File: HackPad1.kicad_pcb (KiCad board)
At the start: 2 copper layers, 3.3 x 3.6 mm, 25 parts, among them J1 Conn_01x04_Pin, SW1 SW_Push, SW10 RotaryEncoder, SW2 SW_Push, SW3 SW_Push, SW4 SW_Push, SW5 SW_Push, SW6 SW_Push, SW7 SW_Push, SW8 SW_Push, SW9 SW_Push, U1 MOUDLE-SEEEDUINO-XIAO

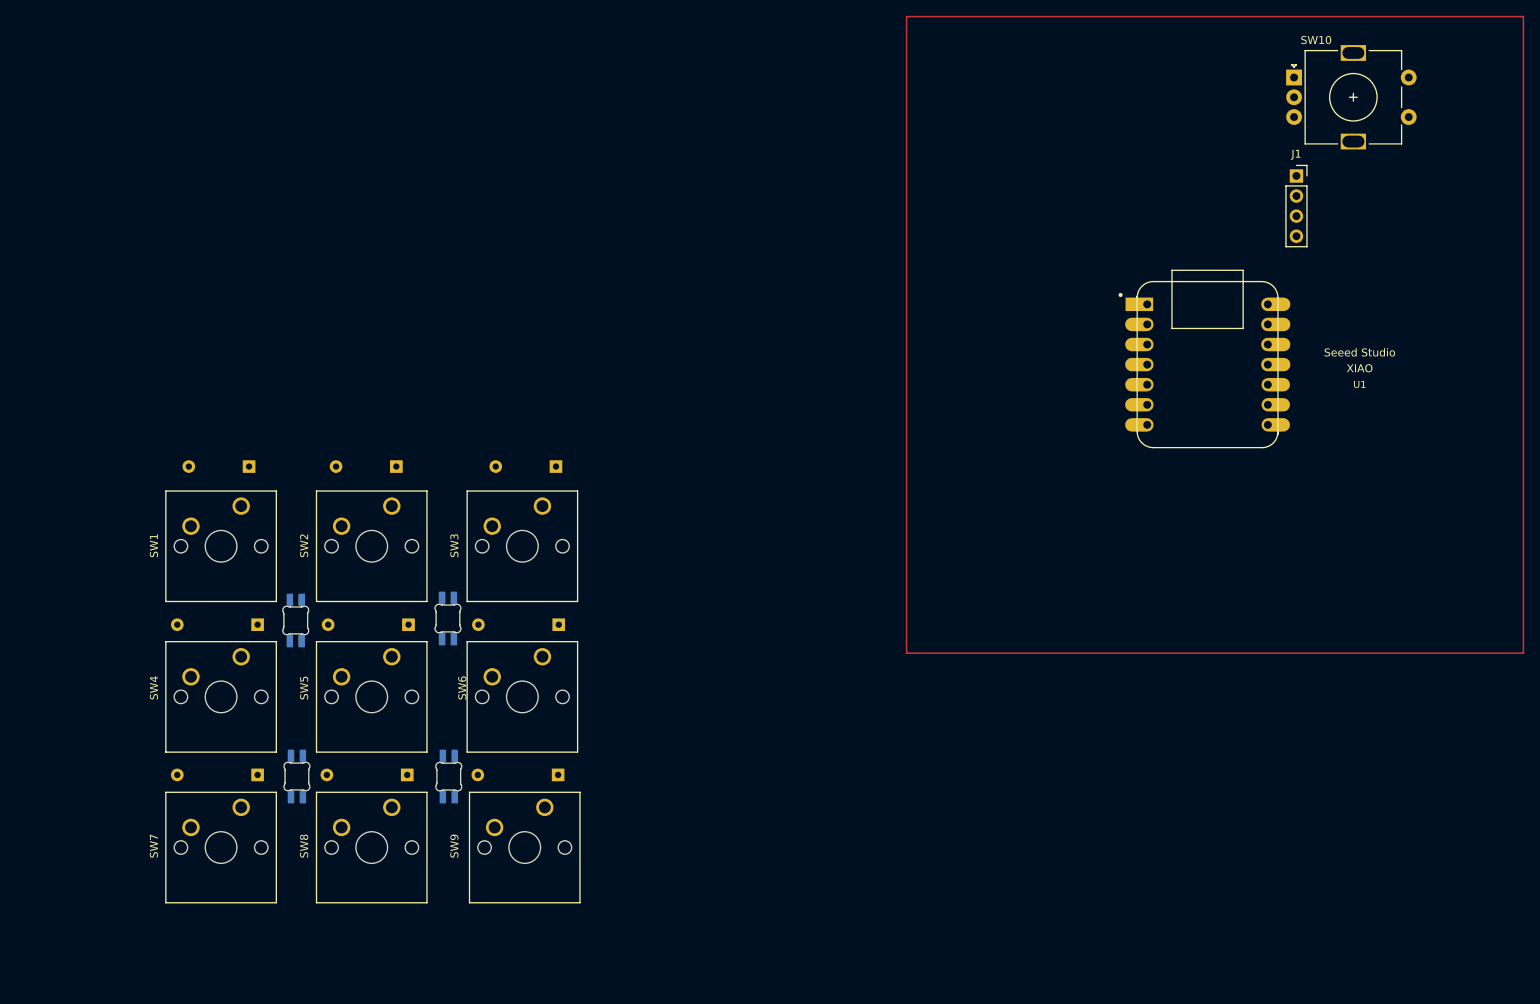
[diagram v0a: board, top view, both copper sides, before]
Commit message: added complete pcb layout need to start routing
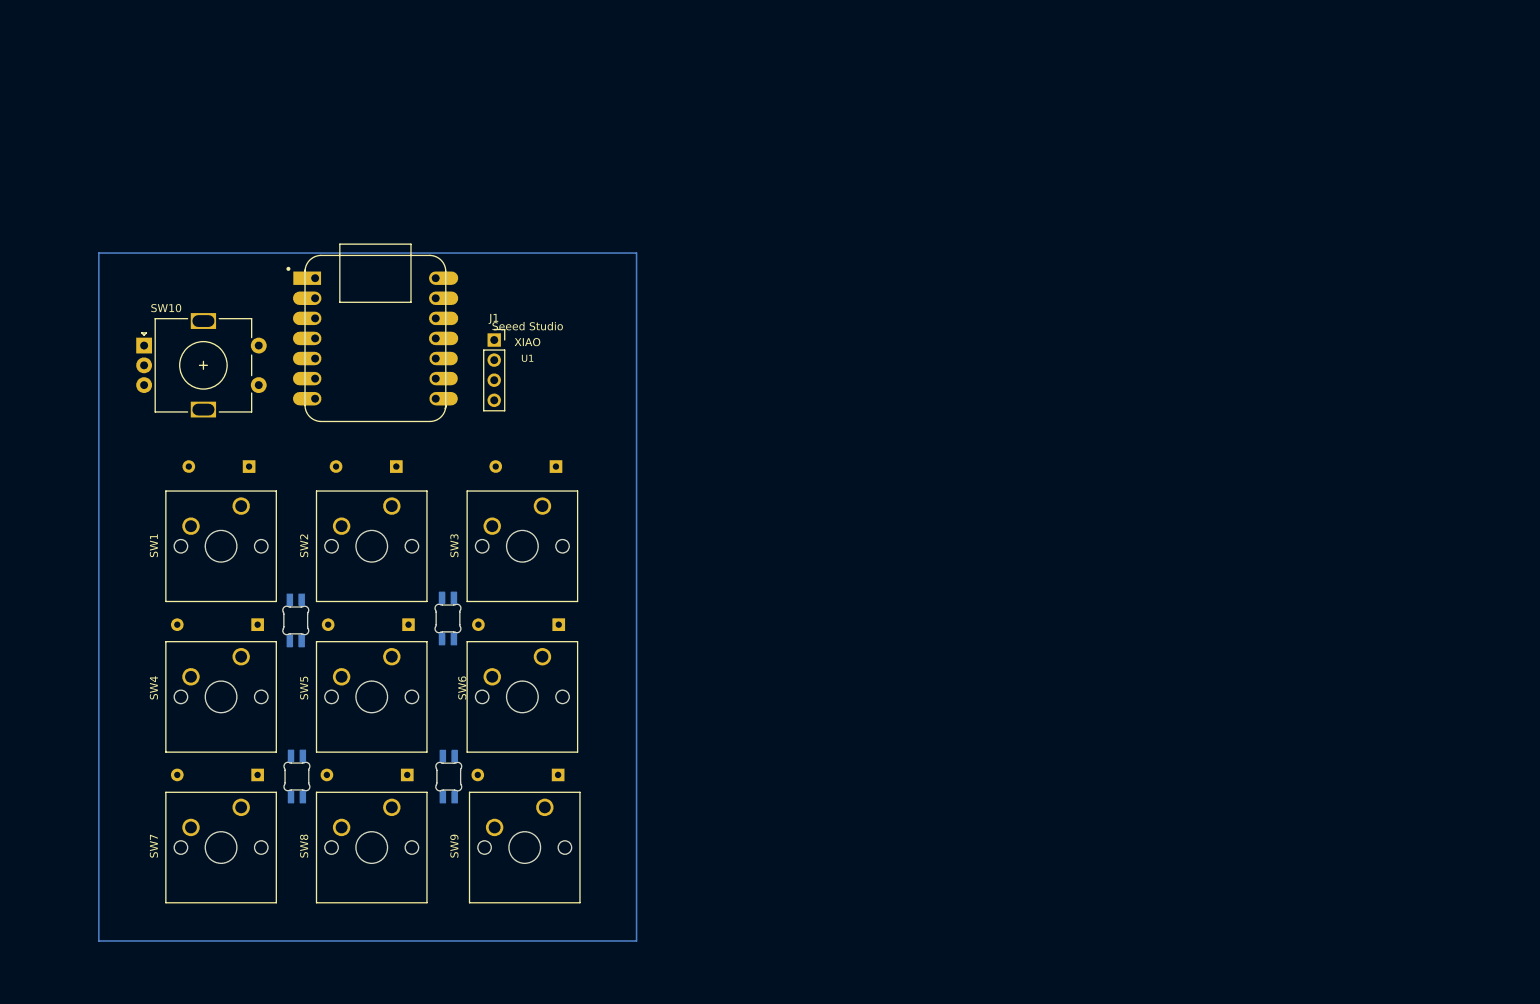
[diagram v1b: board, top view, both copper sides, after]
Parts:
- moved SW10 149.3 mm to (87.7, 79.7)
- moved U1 105.3 mm to (117.0, 78.8)
- moved J1 103.6 mm to (132.0, 79.0)
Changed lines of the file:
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@@
 	(footprint "Rotary_Encoder:RotaryEncoder_Alps_EC11E-Switch_Vertical_H20mm"
 		(layer "F.Cu")
-		(at 233.15 45.8)
+		(at 87.725 79.7)
 		(descr "Alps rotary encoder, EC12E... with switch, vertical shaft, http://www.alps.com/prod/info/E/HTML/Encoder/Incremental/EC11/EC11E15204A3.html")
 		(tags "rotary encoder")
@@
 	(footprint "Connector_PinSocket_2.54mm:PinSocket_1x04_P2.54mm_Vertical"
 		(layer "F.Cu")
-		(at 233.45 58.25)
+		(at 132 79)
 		(descr "Through hole straight socket strip, 1x04, 2.54mm pitch, single row (from Kicad 4.0.7), script generated")
 		(tags "Through hole socket strip THT 1x04 2.54mm single row")
@@
 	(footprint "footprints:XIAO-Generic-Hybrid-14P-2.54-21X17.8MM"
 		(layer "F.Cu")
-		(at 222.209 82.107531)
+		(at 116.975 78.8)
 		(property "Reference" "U1"
 			(at 19.25 2.54 0)
@@
 	)
 	(gr_rect
-		(start 184.15 38.1)
-		(end 262.15 118.6)
+		(start 82 68)
+		(end 150 155)
 		(locked yes)
 		(stroke
@@
 		)
 		(fill none)
-		(layer "F.Cu")
-		(net 23)
+		(layer "B.Cu")
 	)
 )

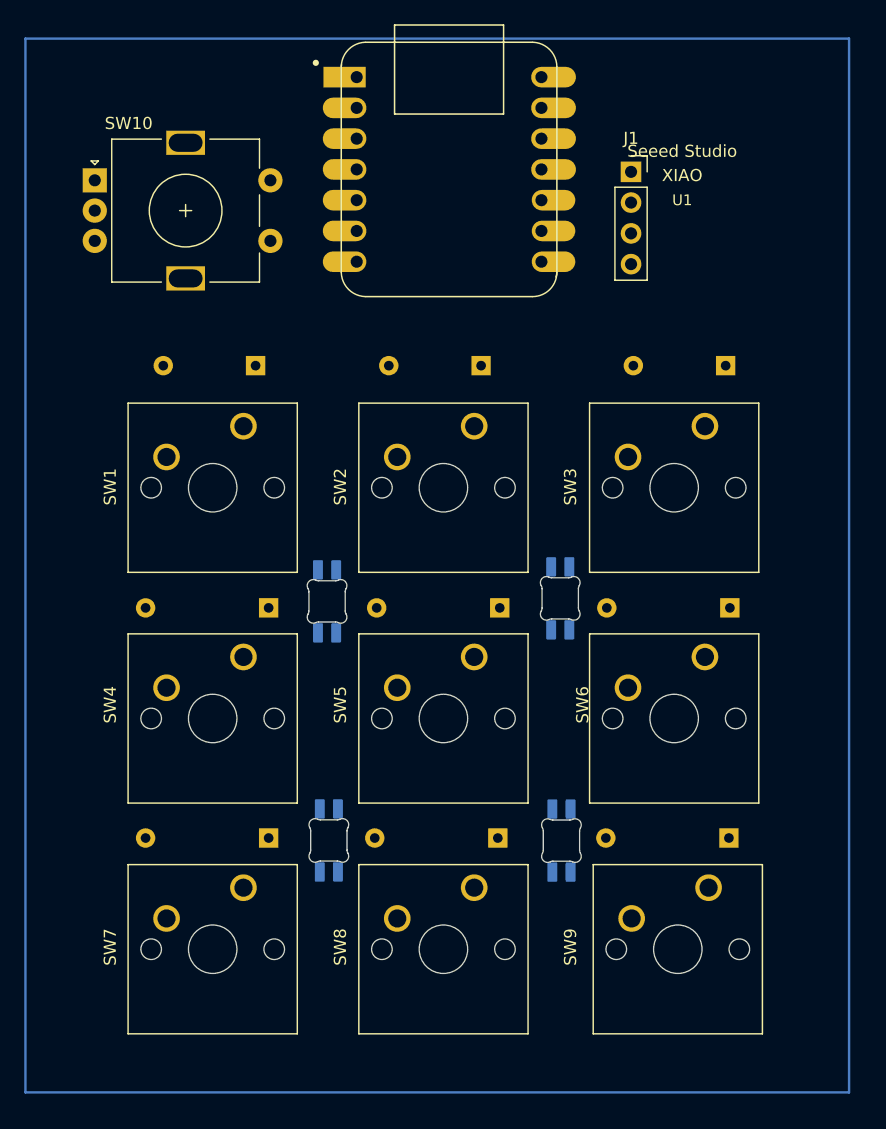
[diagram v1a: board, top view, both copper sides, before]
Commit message: added pcb edge cut
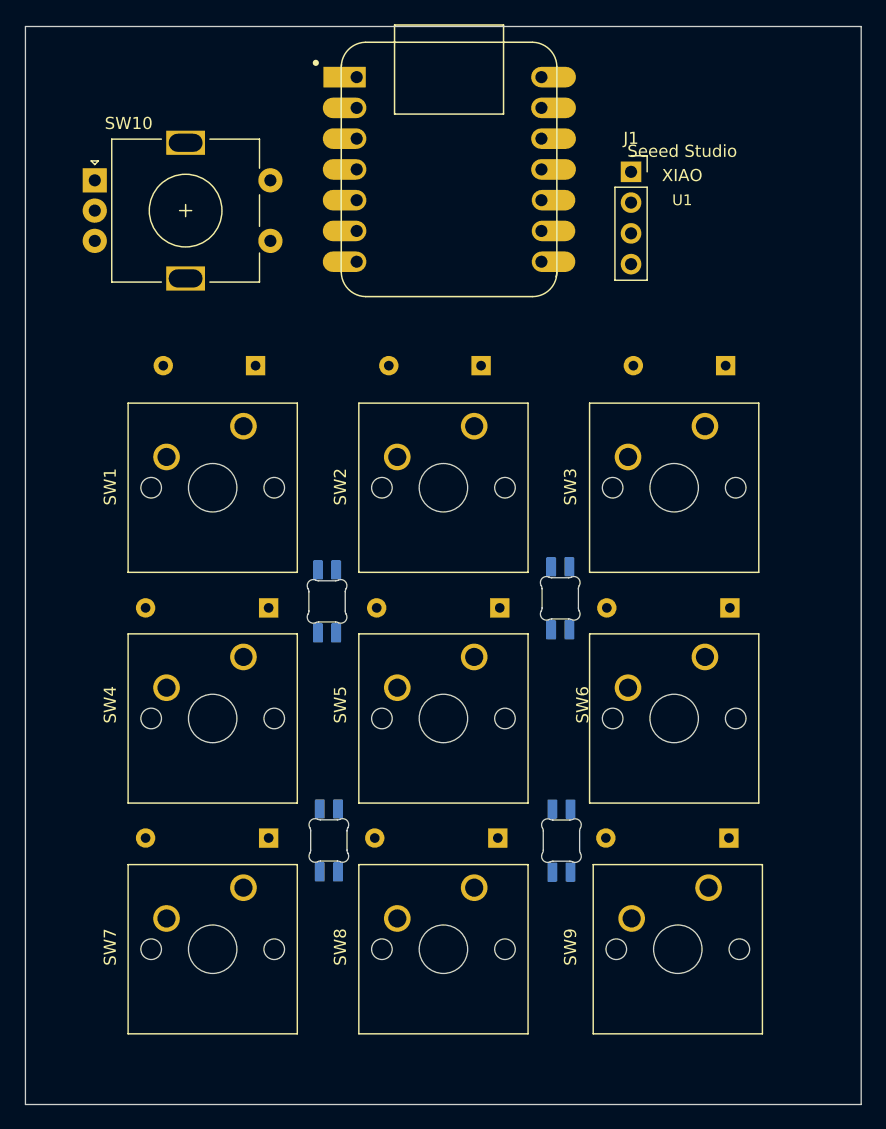
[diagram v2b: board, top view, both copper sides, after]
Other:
- board size 3.3 x 3.6 mm -> 69 x 89 mm
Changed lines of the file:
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@@
 	)
 	(gr_rect
-		(start 82 68)
-		(end 150 155)
-		(locked yes)
+		(start 82 67)
+		(end 151 156)
 		(stroke
-			(width 0.2)
+			(width 0.05)
 			(type default)
 		)
 		(fill none)
-		(layer "B.Cu")
+		(layer "Edge.Cuts")
 	)
 )

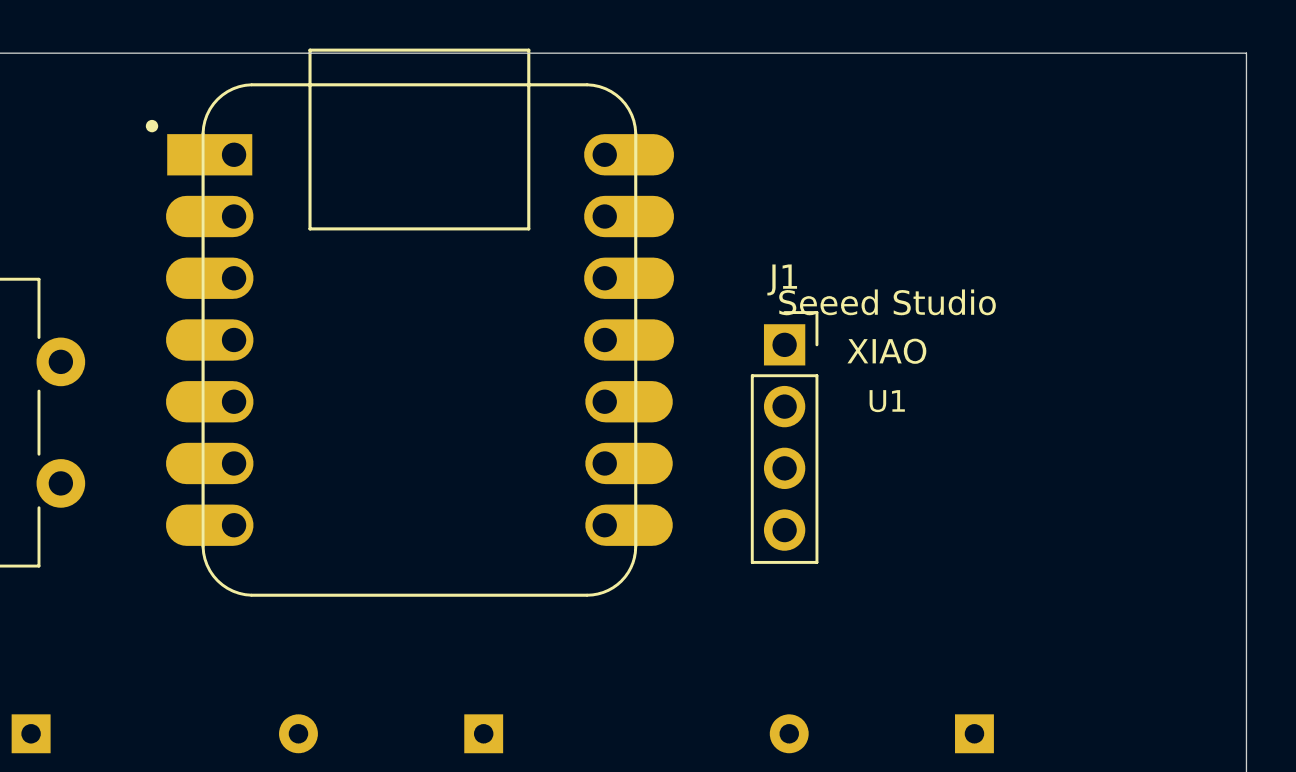
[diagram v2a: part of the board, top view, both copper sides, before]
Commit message: added all 3d models
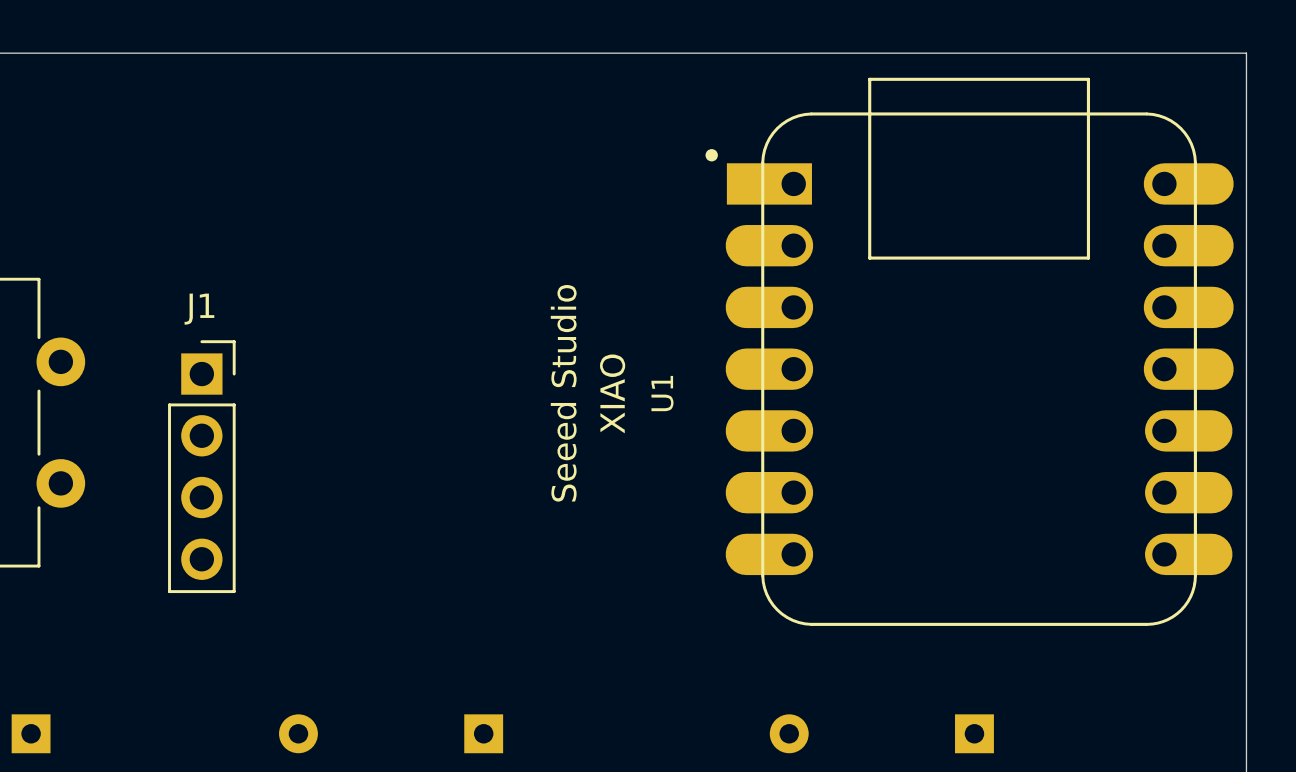
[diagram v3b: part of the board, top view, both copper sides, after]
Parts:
- moved J1 24.0 mm to (108.0, 80.2)
- moved U1 23.1 mm to (140.0, 80.0)

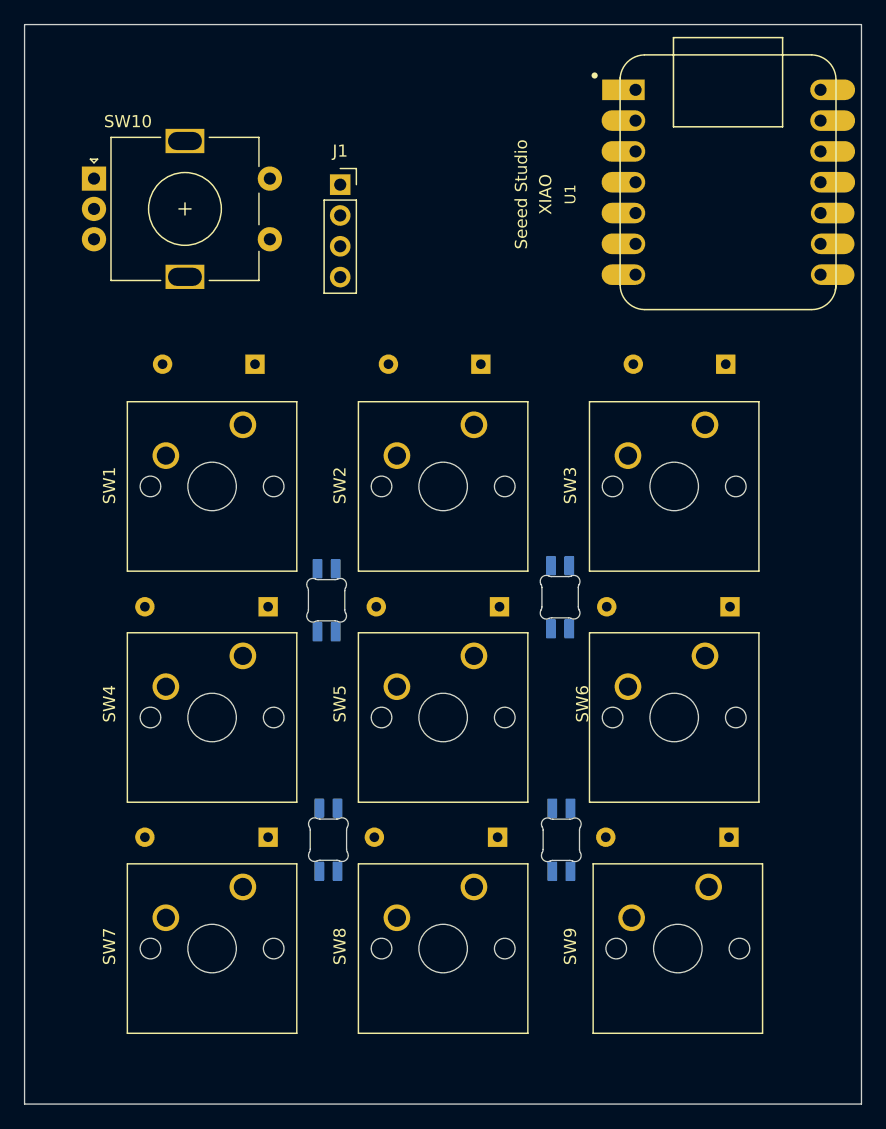
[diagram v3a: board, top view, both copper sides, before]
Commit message: done eouting except power points
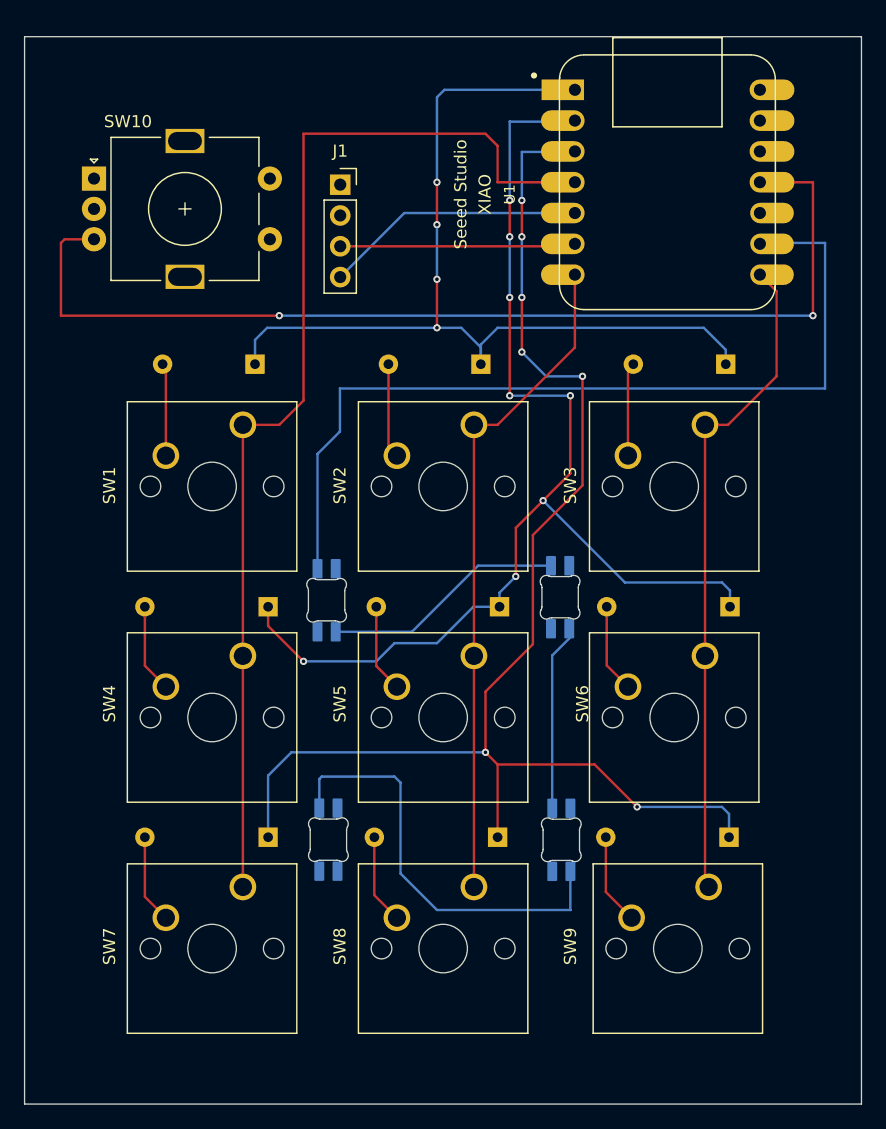
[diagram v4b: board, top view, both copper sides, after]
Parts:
- moved U1 5.00 mm to (135.0, 80.0)
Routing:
- net COL3: track 0.00 -> 114.9 mm, vias 0 -> 7
- net COL2: track 0.00 -> 96.4 mm, vias 0 -> 8
- net ROW1: track 0.00 -> 91.7 mm
- net ENCB: track 0.00 -> 86.2 mm, vias 0 -> 2
- net COL1: track 0.00 -> 78.0 mm, vias 0 -> 4
- net LED_DATA: track 0.00 -> 73.0 mm
- net ROW2: track 0.00 -> 55.1 mm
- net ROW3: track 0.00 -> 54.7 mm
- net Net-(D12-DOUT): track 0.00 -> 35.3 mm
- net SDA: track 0.00 -> 21.5 mm
- net Net-(D10-DOUT): track 0.00 -> 20.0 mm
- net SCL: track 0.00 -> 19.4 mm
- net Net-(D11-DOUT): track 0.00 -> 15.4 mm
- net Net-(D2-A): track 0.00 -> 7.83 mm
- net Net-(D3-A): track 0.00 -> 7.72 mm
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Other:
- board size 69 x 89 mm -> 69 x 88 mm

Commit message: routing done
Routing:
- net +3V3: track 0.00 -> 265.3 mm, vias 0 -> 1
- net ENCA: track 0.00 -> 221.2 mm
- net +5V: track 0.00 -> 198.2 mm, vias 0 -> 8
- added copper zone on B.Cu, net GND
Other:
- board size 69 x 88 mm -> 79 x 89 mm
